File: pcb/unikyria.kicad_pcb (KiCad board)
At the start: 2 copper layers, 58 parts, among them SW1 SW_PUSH, SW10 SW_PUSH, SW11 SW_PUSH, SW12 SW_PUSH, SW13 SW_PUSH, SW14 SW_PUSH, SW15 SW_PUSH, SW16 SW_PUSH, SW17 SW_PUSH, SW18 SW_PUSH, SW19 SW_PUSH, SW2 SW_PUSH, SW20 SW_PUSH, SW22 SW_PUSH, SW23 SW_PUSH, SW24 SW_PUSH, SW25 SW_Push, SW3 SW_PUSH, SW5 SW_PUSH, SW6 SW_PUSH, SW7 SW_PUSH, SW8 SW_PUSH, SW9 SW_PUSH, U1 kb2040, U2 MCP23S17_SO

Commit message: Work on PCBs.
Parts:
- removed D1, D16, D17, D18, D19, D2, D3, D4, D5, D6, D7, D8, D9: 1N4148WT, Diode_SMD:D_SOD-523
- removed H_PAW0: Conn_01x08, Connector_PinHeader_1.00mm:PinHeader_1x08_P1.00mm_Horizontal
- removed JP1, JP2, JP3, JP4, JP5, JP6: SolderJumper_3_Open, Jumper:SolderJumper-3_P2.0mm_Open_TrianglePad1.0x1.5mm
- removed JST_PH_INTC1: Conn_01x12, Connector_JST:JST_PH_S12B-PH-K_1x12_P2.00mm_Horizontal
- removed SW1, SW10, SW11, SW12, SW13, SW14, SW15, SW16, SW17, SW18, SW19, SW2, SW20, SW22, SW23, SW24, SW3, SW5, SW6, SW7, SW8, SW9: SW_PUSH, footprints:CherryMX_Choc_Hotswap
- removed U2: MCP23S17_SO, Package_SO:SOIC-28W_7.5x17.9mm_P1.27mm
- added D00: 1N4148WT, Diode_SMD:D_SOD-523, F.Cu at (-5.00, 12.0)
- added D00B1: 1N4148WT, Diode_SMD:D_SOD-523, B.Cu at (-5.00, 12.0)
- added D01: 1N4148WT, Diode_SMD:D_SOD-523, F.Cu at (13.0, 3.00)
- added D01B1: 1N4148WT, Diode_SMD:D_SOD-523, B.Cu at (13.0, 3.00)
- added D02: 1N4148WT, Diode_SMD:D_SOD-523, F.Cu at (31.0, -6.00)
- added D02B1: 1N4148WT, Diode_SMD:D_SOD-523, B.Cu at (31.0, -6.00)
- added D03: 1N4148WT, Diode_SMD:D_SOD-523, F.Cu at (49.0, 3.00)
- added D03B1: 1N4148WT, Diode_SMD:D_SOD-523, B.Cu at (49.0, 3.00)
- added D04: 1N4148WT, Diode_SMD:D_SOD-523, F.Cu at (67.0, 4.00)
- added D04B1: 1N4148WT, Diode_SMD:D_SOD-523, B.Cu at (67.0, 4.00)
- added D10B1: 1N4148WT, Diode_SMD:D_SOD-523, B.Cu at (-5.00, 30.0)
- added D11B1: 1N4148WT, Diode_SMD:D_SOD-523, B.Cu at (13.0, 21.0)
- added D12B1: 1N4148WT, Diode_SMD:D_SOD-523, B.Cu at (31.0, 12.0)
- added D13B1: 1N4148WT, Diode_SMD:D_SOD-523, B.Cu at (49.0, 21.0)
- added D14B1: 1N4148WT, Diode_SMD:D_SOD-523, B.Cu at (67.0, 21.0)
- added D15B1: 1N4148WT, Diode_SMD:D_SOD-523, B.Cu at (96.2, 44.7)
- added D20B1: 1N4148WT, Diode_SMD:D_SOD-523, B.Cu at (-5.00, 48.0)
- added D21B1: 1N4148WT, Diode_SMD:D_SOD-523, B.Cu at (13.0, 39.0)
- added D22B1: 1N4148WT, Diode_SMD:D_SOD-523, B.Cu at (31.0, 30.0)
- added D23B1: 1N4148WT, Diode_SMD:D_SOD-523, B.Cu at (49.0, 39.0)
- added D24B1: 1N4148WT, Diode_SMD:D_SOD-523, B.Cu at (67.0, 39.0)
- added D25: 1N4148WT, Diode_SMD:D_SOD-523, F.Cu at (90.2, 61.7)
- added D25B1: 1N4148WT, Diode_SMD:D_SOD-523, B.Cu at (90.2, 61.7)
- added D31: 1N4148WT, Diode_SMD:D_SOD-523, F.Cu at (13.0, 57.0)
- added D31B1: 1N4148WT, Diode_SMD:D_SOD-523, B.Cu at (13.0, 57.0)
- added D32: 1N4148WT, Diode_SMD:D_SOD-523, F.Cu at (31.0, 48.0)
- added D32B1: 1N4148WT, Diode_SMD:D_SOD-523, B.Cu at (31.0, 48.0)
- added D33: 1N4148WT, Diode_SMD:D_SOD-523, F.Cu at (49.0, 57.0)
- added D33B1: 1N4148WT, Diode_SMD:D_SOD-523, B.Cu at (49.0, 57.0)
- added D34: 1N4148WT, Diode_SMD:D_SOD-523, F.Cu at (69.7, 57.6)
- added D34B1: 1N4148WT, Diode_SMD:D_SOD-523, B.Cu at (69.7, 57.6)
- added D35: 1N4148WT, Diode_SMD:D_SOD-523, F.Cu at (109.1, 69.8)
- added D35B1: 1N4148WT, Diode_SMD:D_SOD-523, B.Cu at (109.1, 69.8)
- added H_PAW_L1: Conn_01x08, Connector_PinHeader_2.54mm:PinHeader_1x08_P2.54mm_Horizontal, F.Cu at (88.4, 14.7)
- added JST_PH_INTC_L1: Conn_01x12, Connector_JST:JST_PH_S12B-PH-K_1x12_P2.00mm_Horizontal, F.Cu at (127.0, 105.5)
- added MCP_L1: MCP23S17_SO, Package_SO:SOIC-28W_7.5x17.9mm_P1.27mm, F.Cu at (84.2, 96.3)
- added SWL00: SW_PUSH, footprints:ChocV1_V2_Hotswap_18mm, F.Cu at (0.00, 18.0)
- added SWL01: SW_PUSH, footprints:ChocV1_V2_Hotswap_18mm, F.Cu at (18.0, 9.00)
- added SWL02: SW_PUSH, footprints:ChocV1_V2_Hotswap_18mm, F.Cu at (36.0, 0.00)
- added SWL03: SW_PUSH, footprints:ChocV1_V2_Hotswap_18mm, F.Cu at (54.0, 9.00)
- added SWL04: SW_PUSH, footprints:ChocV1_V2_Hotswap_18mm, F.Cu at (72.0, 9.00)
- added SWL10: SW_PUSH, footprints:ChocV1_V2_Hotswap_18mm, F.Cu at (0.00, 36.0)
- added SWL11: SW_PUSH, footprints:ChocV1_V2_Hotswap_18mm, F.Cu at (18.0, 27.0)
- added SWL12: SW_PUSH, footprints:ChocV1_V2_Hotswap_18mm, F.Cu at (36.0, 18.0)
- added SWL13: SW_PUSH, footprints:ChocV1_V2_Hotswap_18mm, F.Cu at (54.0, 27.0)
- added SWL14: SW_PUSH, footprints:ChocV1_V2_Hotswap_18mm, F.Cu at (72.0, 27.0)
- added SWL15: SW_PUSH, footprints:ChocV1_V2_Hotswap_18mm, F.Cu at (98.6, 52.9)
- added SWL20: SW_PUSH, footprints:ChocV1_V2_Hotswap_18mm, F.Cu at (0.00, 54.0)
- added SWL21: SW_PUSH, footprints:ChocV1_V2_Hotswap_18mm, F.Cu at (18.0, 45.0)
- added SWL22: SW_PUSH, footprints:ChocV1_V2_Hotswap_18mm, F.Cu at (36.0, 36.0)
- added SWL23: SW_PUSH, footprints:ChocV1_V2_Hotswap_18mm, F.Cu at (54.0, 45.0)
- added SWL24: SW_PUSH, footprints:ChocV1_V2_Hotswap_18mm, F.Cu at (72.0, 45.0)
- added SWL25: SW_PUSH, footprints:ChocV1_V2_Hotswap_18mm, F.Cu at (92.5, 69.8)
- added SWL31: SW_PUSH, footprints:ChocV1_V2_Hotswap_18mm, F.Cu at (18.0, 63.0)
- added SWL32: SW_PUSH, footprints:ChocV1_V2_Hotswap_18mm, F.Cu at (36.0, 54.0)
- added SWL33: SW_PUSH, footprints:ChocV1_V2_Hotswap_18mm, F.Cu at (54.0, 63.0)
- added SWL34: SW_PUSH, footprints:ChocV1_V2_Hotswap_18mm, F.Cu at (73.5, 64.7)
- added SWL35: SW_PUSH, footprints:ChocV1_V2_Hotswap_18mm, F.Cu at (110.2, 78.1)
- U1: value kb2040 -> ProMicro
- moved JST_PH_BATT1 247.6 mm to (184.0, 79.0)
- moved U1 234.3 mm to (140.6, 14.4)
- moved SW25 224.1 mm to (160.0, -1.50)
- moved D15 155.2 mm to (96.2, 44.7), turned to -20 degrees
- moved D14 125.8 mm to (67.0, 21.0)
- moved D24 120.9 mm to (67.0, 39.0)
- moved D13 107.7 mm to (49.0, 21.0)
- moved D23 104.0 mm to (49.0, 39.0)
- moved D12 90.1 mm to (31.0, 12.0)
- moved D22 84.9 mm to (31.0, 30.0)
- moved D11 71.8 mm to (13.0, 21.0)
- moved D21 69.6 mm to (13.0, 39.0)
- moved D20 56.3 mm to (-5.00, 48.0)
- moved D10 55.8 mm to (-5.00, 30.0)
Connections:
- D13 pad 1: /R2 -> /R1
- D14 pad 1: /R2 -> /R1
- D15 pad 1: /R2 -> /R1
- D20 pad 1: /R3 -> /R2
- D21 pad 1: /R3 -> /R2
- D22 pad 1: /R3 -> /R2
- D23 pad 1: /R3 -> /R2
- D24 pad 1: /R3 -> /R2
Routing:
- net /R1: track 0.00 -> 128.9 mm
- net /C4: track 0.00 -> 128.9 mm
- net /C1: track 0.00 -> 128.0 mm
- net /C3: track 0.00 -> 128.0 mm
- net /C2: track 0.00 -> 128.0 mm
- net /R2: track 0.00 -> 125.8 mm
- net /R3: track 0.00 -> 124.6 mm
- net /C5: track 0.00 -> 109.1 mm
- net /C0: track 0.00 -> 94.1 mm
- net /R0: track 0.00 -> 87.5 mm
- net Net-(D23-A): track 0.00 -> 35.6 mm
- net Net-(D15-A): track 0.00 -> 35.2 mm
- net Net-(D25-A): track 0.00 -> 35.0 mm
- net Net-(D10-A): track 0.00 -> 34.6 mm
- net Net-(D35-A): track 0.00 -> 34.3 mm
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- added copper zone on B.Cu, net GND
- added copper zone on F.Cu, net GND
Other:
- board outline added: 143 x 110.6 mm

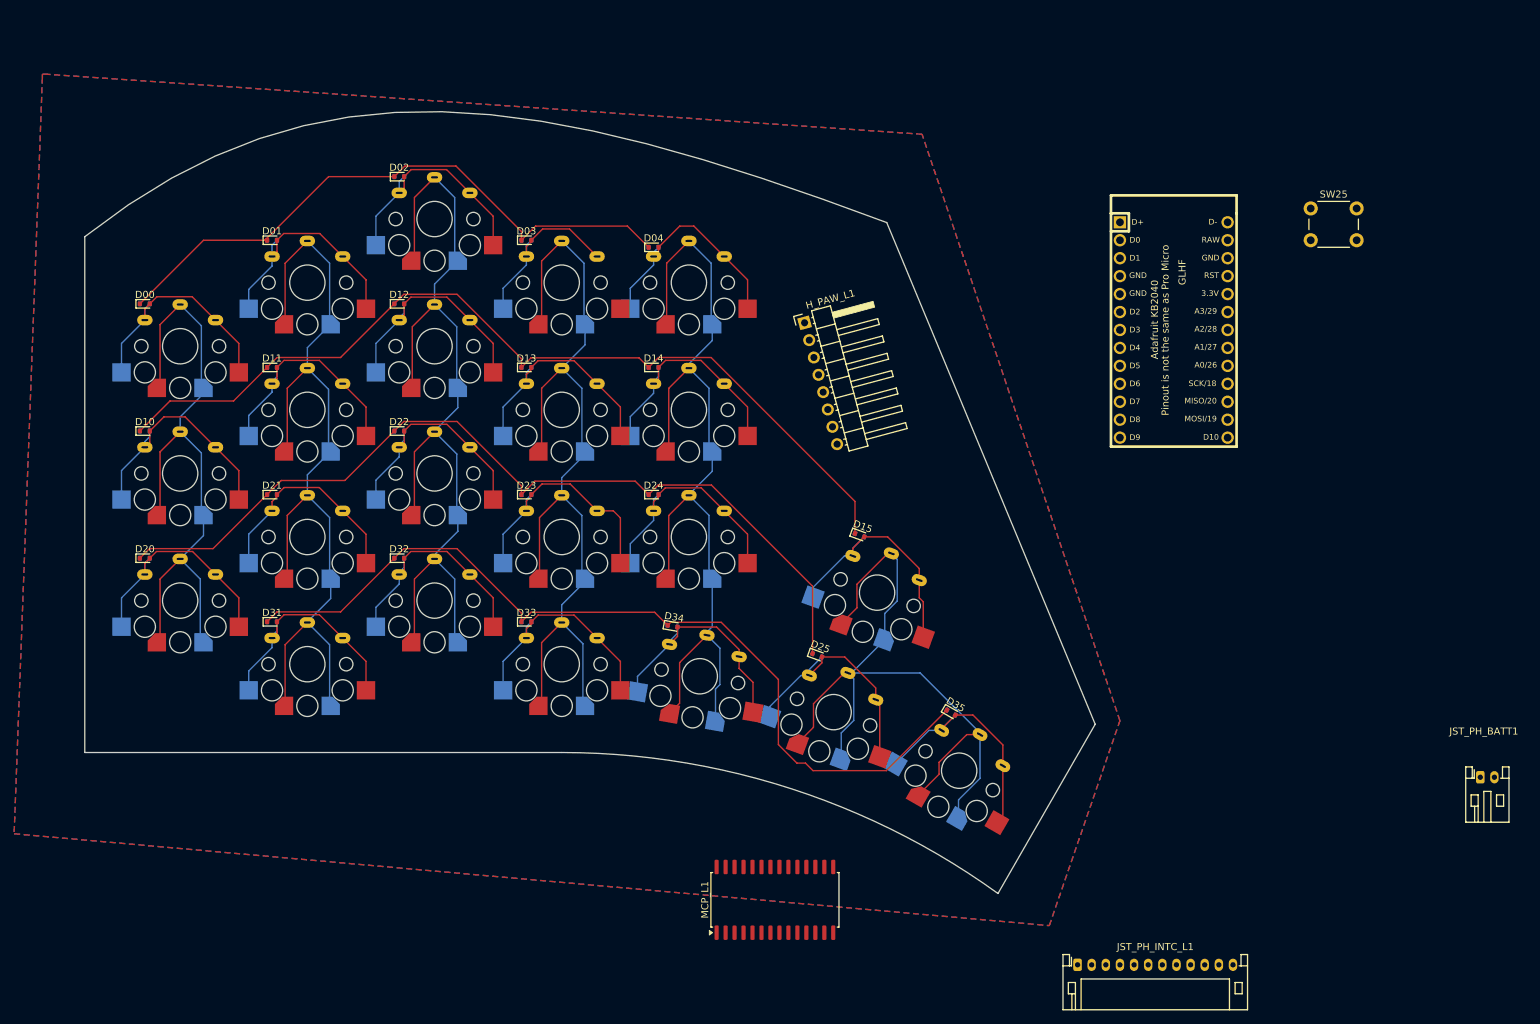
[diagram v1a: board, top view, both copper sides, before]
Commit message: Replace KB2040 with XIAO nRF, work on PCB routing.
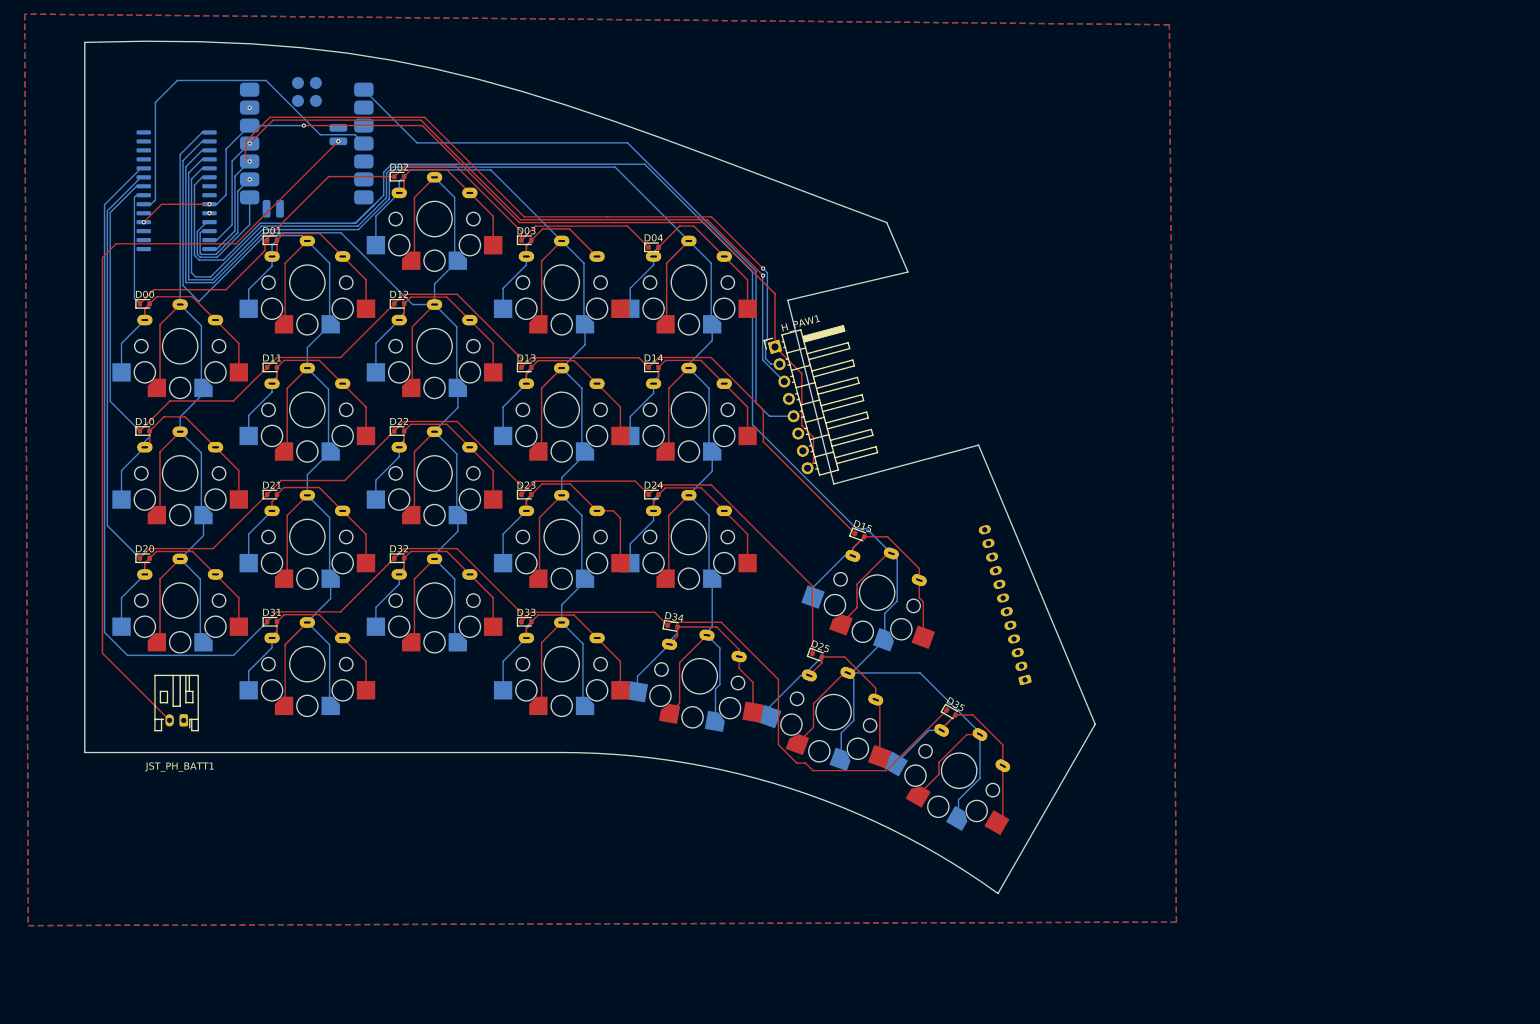
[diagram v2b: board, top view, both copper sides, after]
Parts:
- removed SW25: SW_Push, Button_Switch_THT:SW_PUSH_6mm
- removed U1: ProMicro, footprints:kb2040
- added U2: XIAO-nRF52840-SMD, footprints:XIAO-nRF52840-SMD, B.Cu at (17.9, -10.7)
- JST_PH_INTC1: renamed from JST_PH_INTC_L1; moved to B.Cu
- MCP1: renamed from MCP_L1; moved to B.Cu
- moved JST_PH_BATT1 183.7 mm to (0.50, 71.0), turned to 180 degrees
- moved MCP1 131.3 mm to (-0.50, -4.00), turned to 180 degrees
- moved JST_PH_INTC1 41.0 mm to (119.6, 65.2), turned to 105 degrees
- moved H_PAW1 5.40 mm to (84.2, 18.1)
- renumbered H_PAW_L1 to H_PAW1
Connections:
- H_PAW1 pad 8: /RST1 -> +3.3V
- JST_PH_INTC1 pad 10: /RST3 -> unconnected-(JST_PH_INTC1-Pin_10-Pad10)
- JST_PH_INTC1 pad 9: /RST2 -> unconnected-(JST_PH_INTC1-Pin_9-Pad9)
- MCP1 pad 18: /RST0 -> +3.3V
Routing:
- net /C5: track 109.1 -> 267.6 mm
- net +3.3V: track 0.00 -> 136.3 mm, vias 0 -> 3
- net /MISO: track 0.00 -> 117.4 mm, vias 0 -> 2
- net /MOSI: track 0.00 -> 116.1 mm, vias 0 -> 2
- net +BATT: track 0.00 -> 109.6 mm, vias 0 -> 1
- net /C4: track 128.9 -> 228.7 mm
- net /R3: track 124.6 -> 219.2 mm
- net /CS1: track 0.00 -> 90.9 mm
- net /C3: track 128.0 -> 212.3 mm
- net /C2: track 128.0 -> 191.1 mm
- net /R2: track 125.8 -> 184.0 mm
- net /INT0: track 0.00 -> 50.2 mm
- net /C1: track 128.0 -> 173.3 mm
- net /R1: track 128.9 -> 167.8 mm
- net /C0: track 94.1 -> 120.8 mm
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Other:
- board size 143 x 110.6 mm -> 143 x 120.6 mm
